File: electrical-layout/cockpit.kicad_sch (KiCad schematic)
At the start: 10 parts, among them SW2 Start Button, SW3 Stop Button, SW4 Dead Man's Switch, SW5 Emergency Stop Button, U5 PCB Cockpit, U6 Raspberry Pi 4B+, U7 Pilot Display, U8 Arduino MKR NB 1500

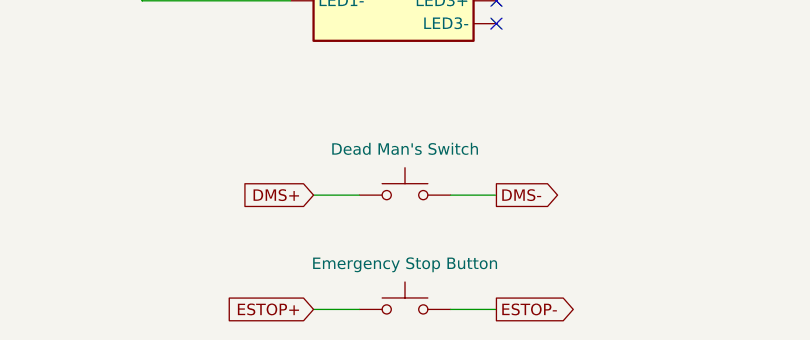
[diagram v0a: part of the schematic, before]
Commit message: layout-2025: change to version 3.0
A few changes were made for this new version:
- Version and dates were changed on all sheets
- Added a switch (temporary symbol) after the telemetry battery
- A few notes were removed, as these have either been resolved or
discussed somewhere else
- Changed battery symbol to multi-cell battery
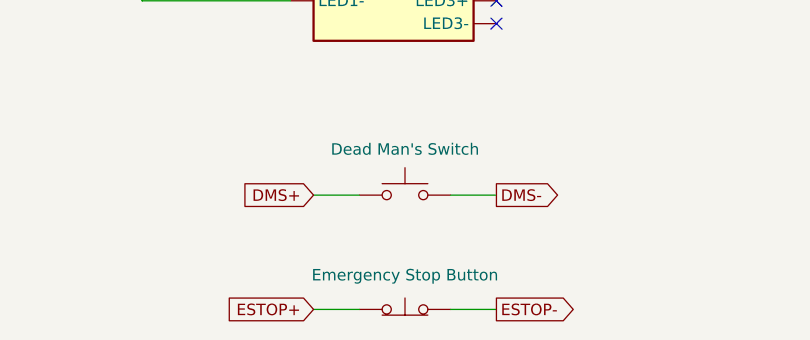
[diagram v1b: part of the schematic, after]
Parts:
- removed SW5: Emergency Stop Button, symbol Switch:SW_Push
- added SW6: Emergency Stop Button, symbol Switch:SW_Push_Open
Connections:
- net ESTOP+: now also SW6.1 (A)
- net ESTOP-: now also SW6.2 (B)
- net at U7. (HDMI): now also U6. (GND)
- net at U6. (GND): no longer U7. (HDMI)
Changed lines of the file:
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@@
 	(title_block
 		(title "Cockpit")
-		(date "2025-07-15")
-		(rev "v0.1.0")
+		(date "2025-09-06")
+		(rev "v0.3.0")
 	)
 	(junction
@@
 	)
 	(symbol
+		(lib_id "Switch:SW_Push_Open")
+		(at 118.11 151.13 0)
+		(unit 1)
+		(exclude_from_sim no)
+		(in_bom yes)
+		(on_board yes)
+		(dnp no)
+		(fields_autoplaced yes)
+		(property "Reference" "SW6"
+			(at 118.11 144.78 0)
+			(effects
+				(font
+					(size 1.27 1.27)
+				)
+				(hide yes)
+			)
+		)
+		(property "Value" "Emergency Stop Button"
+			(at 118.11 147.32 0)
+			(effects
+				(font
+					(size 1.27 1.27)
+				)
+			)
+		)
+		(property "Footprint" ""
+			(at 118.11 146.05 0)
+			(effects
+				(font
+					(size 1.27 1.27)
+				)
+				(hide yes)
+			)
+		)
+		(property "Datasheet" "~"
+			(at 118.11 146.05 0)
+			(effects
+				(font
+					(size 1.27 1.27)
+				)
+				(hide yes)
+			)
+		)
+		(property "Description" "Push button switch, push-to-open, generic, two pins"
+			(at 118.11 151.13 0)
+			(effects
+				(font
+					(size 1.27 1.27)
+				)
+				(hide yes)
+			)
+		)
+		(pin "2"
+		)
+		(pin "1"
+		)
+		(instances
+			(project ""
+				(path "/3f5ae950-00dd-4aca-9f75-0d872ff9560e/86f73561-33e7-4ee1-aeca-93be9f30f6f7"
+					(reference "SW6")
+					(unit 1)
+				)
+			)
+		)
+	)
+	(symbol
 		(lib_id "Device:LED")
 		(at 96.52 114.3 0)
@@
 					(unit 1)
 				)
-			)
-		)
-	)
-	(symbol
-		(lib_id "Switch:SW_Push")
-		(at 118.11 151.13 0)
-		(unit 1)
-		(exclude_from_sim no)
-		(in_bom yes)
-		(on_board yes)
-		(dnp no)
-		(fields_autoplaced yes)
-		(property "Reference" "SW5"
-			(at 118.11 143.51 0)
-			(effects
-				(font
-					(size 1.27 1.27)
-				)
-				(hide yes)
-			)
-		)
-		(property "Value" "Emergency Stop Button"
-			(at 118.11 146.05 0)
-			(effects
-				(font
-					(size 1.27 1.27)
-				)
-			)
-		)
-		(property "Footprint" ""
-			(at 118.11 146.05 0)
-			(effects
-				(font
-					(size 1.27 1.27)
-				)
-				(hide yes)
-			)
-		)
-		(property "Datasheet" "~"
-			(at 118.11 146.05 0)
-			(effects
-				(font
-					(size 1.27 1.27)
-				)
-				(hide yes)
-			)
-		)
-		(property "Description" "Push button switch, generic, two pins"
-			(at 118.11 151.13 0)
-			(effects
-				(font
-					(size 1.27 1.27)
-				)
-				(hide yes)
-			)
-		)
-		(pin "1"
-		)
-		(pin "2"
-		)
-		(instances
-			(project ""
-				(path "/3f5ae950-00dd-4aca-9f75-0d872ff9560e/86f73561-33e7-4ee1-aeca-93be9f30f6f7"
-					(reference "SW5")
-					(unit 1)
-				)
